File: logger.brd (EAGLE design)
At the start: 99 x 44.1 mm, 69 parts, among them IC1 LTC4412, J1 POWER_JACKPTH, Q1 FDN360P, Q2 FDN360P, Q3 2N7002PW, Q4 2N7002PW, U1 FT232RL

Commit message: Vcl attached to clock power and communication
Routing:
- net VDD: track 143.4 -> 128.8 mm, vias 3 -> 5
- net VCL: track 22.8 -> 29.2 mm
- net GND: vias 43 -> 48

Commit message: Vcl attached to clock power and communication
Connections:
- new net D4-SENSE_3V3_SWITCH: MCU.2, SENSE.3, TPS6122.6
- net D6-CLOCK_3V3_SWITCH: no longer MCU.2, SENSE.3, TPS6122.6
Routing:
- net D4-SENSE_3V3_SWITCH: track 0.00 -> 97.8 mm, vias 0 -> 6
- net D6-CLOCK_3V3_SWITCH: track 45.7 -> 43.3 mm, vias 4 -> 8
- net GND: vias 48 -> 50
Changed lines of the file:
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@@
 </signal>
 <signal name="D6-CLOCK_3V3_SWITCH">
-<contactref element="SENSE" pad="3"/>
-<contactref element="MCU" pad="2"/>
 <contactref element="CLOCK" pad="3"/>
 <contactref element="MCU" pad="10"/>
-<contactref element="TPS6122" pad="6"/>
-<wire x1="70.866" y1="15.8496" x2="71.4756" y2="15.8496" width="0.2032" layer="1"/>
-<wire x1="69.6468" y1="17.0688" x2="70.866" y2="15.8496" width="0.2032" layer="1"/>
-<wire x1="62.9412" y1="17.0688" x2="69.6468" y2="17.0688" width="0.2032" layer="1"/>
-<wire x1="60.5028" y1="17.0688" x2="62.9412" y2="17.0688" width="0.2032" layer="16"/>
-<wire x1="59.7408" y1="17.0688" x2="60.5028" y2="17.0688" width="0.2032" layer="1"/>
-<wire x1="57.3024" y1="14.6304" x2="59.7408" y2="17.0688" width="0.2032" layer="1"/>
-<wire x1="55.7784" y1="14.6304" x2="57.3024" y2="14.6304" width="0.2032" layer="1"/>
-<wire x1="55.3212" y1="14.1732" x2="55.7784" y2="14.6304" width="0.2032" layer="16"/>
-<wire x1="53.9369" y1="14.8082" x2="55.3212" y2="14.1732" width="0.2032" layer="16"/>
-<wire x1="53.9623" y1="14.8082" x2="53.9369" y2="14.8082" width="0.2032" layer="1"/>
-<wire x1="53.1876" y1="13.716" x2="53.9623" y2="14.8082" width="0.2032" layer="1"/>
-<wire x1="71.4756" y1="15.8496" x2="71.5516" y2="15.7663" width="0.2032" layer="1"/>
+<wire x1="54.2544" y1="14.7828" x2="53.1876" y2="13.716" width="0.2032" layer="1"/>
+<wire x1="55.626" y1="14.7828" x2="54.2544" y2="14.7828" width="0.2032" layer="16"/>
+<wire x1="55.7784" y1="14.6304" x2="55.626" y2="14.7828" width="0.2032" layer="16"/>
+<wire x1="57.3024" y1="14.6304" x2="55.7784" y2="14.6304" width="0.2032" layer="1"/>
+<wire x1="59.5884" y1="16.9164" x2="57.3024" y2="14.6304" width="0.2032" layer="1"/>
+<wire x1="60.5028" y1="16.9164" x2="59.5884" y2="16.9164" width="0.2032" layer="1"/>
+<wire x1="62.9412" y1="16.9164" x2="60.5028" y2="16.9164" width="0.2032" layer="16"/>
+<wire x1="62.9412" y1="19.9644" x2="62.9412" y2="16.9164" width="0.2032" layer="1"/>
+<wire x1="62.9412" y1="22.2504" x2="62.9412" y2="19.9644" width="0.2032" layer="16"/>
+<wire x1="61.2648" y1="23.9268" x2="62.9412" y2="22.2504" width="0.2032" layer="16"/>
+<wire x1="61.2648" y1="30.7848" x2="61.2648" y2="23.9268" width="0.2032" layer="16"/>
+<wire x1="60.5028" y1="31.5468" x2="61.2648" y2="30.7848" width="0.2032" layer="16"/>
+<wire x1="58.674" y1="31.5468" x2="60.5028" y2="31.5468" width="0.2032" layer="1"/>
+<wire x1="53.9496" y1="26.8224" x2="58.674" y2="31.5468" width="0.2032" layer="1"/>
+<wire x1="51.9684" y1="26.8224" x2="53.9496" y2="26.8224" width="0.2032" layer="1"/>
+<wire x1="51.3588" y1="26.2128" x2="51.9684" y2="26.8224" width="0.2032" layer="1"/>
+<wire x1="51.3588" y1="24.0792" x2="51.3588" y2="26.2128" width="0.2032" layer="16"/>
+<wire x1="50.4444" y1="23.1648" x2="51.3588" y2="24.0792" width="0.2032" layer="16"/>
+<wire x1="49.8348" y1="23.7744" x2="50.4444" y2="23.1648" width="0.2032" layer="1"/>
+<wire x1="49.8348" y1="24.384" x2="49.8348" y2="23.7744" width="0.2032" layer="1"/>
 <wire x1="53.1876" y1="13.716" x2="53.0525" y2="13.65" width="0.2032" layer="1"/>
-<wire x1="40.5384" y1="14.0462" x2="40.0812" y2="13.4112" width="0.2032" layer="1"/>
-<wire x1="43.8912" y1="16.764" x2="40.5384" y2="14.0462" width="0.2032" layer="1"/>
-<wire x1="44.5008" y1="16.764" x2="43.8912" y2="16.764" width="0.2032" layer="1"/>
-<wire x1="47.117" y1="18.7452" x2="46.482" y2="18.2245" width="0.2032" layer="1"/>
-<wire x1="46.482" y1="18.2245" x2="45.72" y2="17.145" width="0.2032" layer="1"/>
-<wire x1="45.72" y1="17.145" x2="44.5008" y2="16.764" width="0.2032" layer="1"/>
-<wire x1="50.9016" y1="18.7452" x2="49.8348" y2="18.7452" width="0.2032" layer="1"/>
-<wire x1="49.8348" y1="18.7452" x2="47.117" y2="18.7452" width="0.2032" layer="1"/>
-<wire x1="51.3588" y1="18.288" x2="50.9016" y2="18.7452" width="0.2032" layer="1"/>
-<wire x1="51.9684" y1="18.288" x2="51.3588" y2="18.288" width="0.2032" layer="1"/>
-<wire x1="40.0812" y1="13.4112" x2="40.035" y2="13.3325" width="0.2032" layer="1"/>
-<wire x1="51.9684" y1="18.288" x2="52.0827" y2="18.1676" width="0.2032" layer="1"/>
-<wire x1="49.8348" y1="18.7452" x2="49.8348" y2="24.384" width="0.2032" layer="1"/>
 <wire x1="49.8348" y1="24.384" x2="49.7901" y2="24.4602" width="0.2032" layer="1"/>
-<wire x1="53.9369" y1="14.7574" x2="53.9369" y2="14.8082" width="0.2032" layer="1"/>
-<wire x1="53.7972" y1="15.8496" x2="53.9369" y2="14.7574" width="0.2032" layer="1"/>
-<wire x1="53.7972" y1="17.0688" x2="53.7972" y2="15.8496" width="0.2032" layer="1"/>
-<wire x1="52.7304" y1="18.1356" x2="53.7972" y2="17.0688" width="0.2032" layer="1"/>
-<wire x1="52.1208" y1="18.1356" x2="52.7304" y2="18.1356" width="0.2032" layer="1"/>
-<wire x1="52.1208" y1="18.1356" x2="52.0827" y2="18.1676" width="0.2032" layer="1"/>
-<via x="62.9412" y="17.0688" extent="1-16" drill="0.3048"/>
-<via x="60.5028" y="17.0688" extent="1-16" drill="0.3048"/>
+<via x="54.2544" y="14.7828" extent="1-16" drill="0.3048"/>
 <via x="55.7784" y="14.6304" extent="1-16" drill="0.3048"/>
-<via x="53.9369" y="14.8082" extent="1-16" drill="0.3048"/>
+<via x="60.5028" y="16.9164" extent="1-16" drill="0.3048"/>
+<via x="62.9412" y="16.9164" extent="1-16" drill="0.3048"/>
+<via x="62.9412" y="19.9644" extent="1-16" drill="0.3048"/>
+<via x="60.5028" y="31.5468" extent="1-16" drill="0.3048"/>
+<via x="51.3588" y="26.2128" extent="1-16" drill="0.3048"/>
+<via x="50.4444" y="23.1648" extent="1-16" drill="0.3048"/>
 </signal>
 <signal name="LED+">
@@
 <via x="32.385" y="8.5725" extent="1-16" drill="0.3048" shape="octagon"/>
 <via x="80.3275" y="13.0175" extent="1-16" drill="0.3048" shape="octagon"/>
+<via x="37.1475" y="6.35" extent="1-16" drill="0.3048" shape="octagon"/>
+<via x="52.705" y="33.3375" extent="1-16" drill="0.3048" shape="octagon"/>
 </signal>
 <signal name="5V">
@@
 <via x="62.9412" y="13.1064" extent="1-16" drill="0.3048"/>
 </signal>
+<signal name="D4-SENSE_3V3_SWITCH">
+<contactref element="TPS6122" pad="6"/>
+<contactref element="MCU" pad="2"/>
+<contactref element="SENSE" pad="3"/>
+<wire x1="70.866" y1="15.8496" x2="71.4756" y2="15.8496" width="0.2032" layer="1"/>
+<wire x1="69.342" y1="17.3736" x2="70.866" y2="15.8496" width="0.2032" layer="1"/>
+<wire x1="69.342" y1="37.338" x2="69.342" y2="17.3736" width="0.2032" layer="16"/>
+<wire x1="63.0936" y1="43.5864" x2="69.342" y2="37.338" width="0.2032" layer="16"/>
+<wire x1="44.8056" y1="43.5864" x2="63.0936" y2="43.5864" width="0.2032" layer="16"/>
+<wire x1="41.7576" y1="40.5384" x2="44.8056" y2="43.5864" width="0.2032" layer="16"/>
+<wire x1="41.7576" y1="35.6616" x2="41.7576" y2="40.5384" width="0.2032" layer="16"/>
+<wire x1="41.6052" y1="35.5092" x2="41.7576" y2="35.6616" width="0.2032" layer="16"/>
+<wire x1="41.6052" y1="34.7472" x2="41.6052" y2="35.5092" width="0.2032" layer="1"/>
+<wire x1="44.8056" y1="31.5468" x2="41.6052" y2="34.7472" width="0.2032" layer="1"/>
+<wire x1="44.8056" y1="30.6324" x2="44.8056" y2="31.5468" width="0.2032" layer="16"/>
+<wire x1="43.8912" y1="29.718" x2="44.8056" y2="30.6324" width="0.2032" layer="16"/>
+<wire x1="44.196" y1="29.718" x2="43.8912" y2="29.718" width="0.2032" layer="1"/>
+<wire x1="44.3484" y1="29.5656" x2="44.196" y2="29.718" width="0.2032" layer="1"/>
+<wire x1="46.482" y1="29.5656" x2="44.3484" y2="29.5656" width="0.2032" layer="1"/>
+<wire x1="46.6344" y1="29.4132" x2="46.482" y2="29.5656" width="0.2032" layer="1"/>
+<wire x1="47.3964" y1="29.4132" x2="46.6344" y2="29.4132" width="0.2032" layer="16"/>
+<wire x1="50.4444" y1="26.3652" x2="47.3964" y2="29.4132" width="0.2032" layer="16"/>
+<wire x1="50.4444" y1="24.2316" x2="50.4444" y2="26.3652" width="0.2032" layer="16"/>
+<wire x1="49.6824" y1="23.4696" x2="50.4444" y2="24.2316" width="0.2032" layer="16"/>
+<wire x1="49.6824" y1="20.7264" x2="49.6824" y2="23.4696" width="0.2032" layer="16"/>
+<wire x1="49.6824" y1="19.9644" x2="49.6824" y2="20.7264" width="0.2032" layer="1"/>
+<wire x1="51.3588" y1="18.288" x2="50.9016" y2="18.7452" width="0.2032" layer="1"/>
+<wire x1="50.9016" y1="18.7452" x2="49.6824" y2="19.9644" width="0.2032" layer="1"/>
+<wire x1="51.9684" y1="18.288" x2="51.3588" y2="18.288" width="0.2032" layer="1"/>
+<wire x1="71.4756" y1="15.8496" x2="71.5516" y2="15.7663" width="0.2032" layer="1"/>
+<wire x1="51.9684" y1="18.288" x2="52.0827" y2="18.1676" width="0.2032" layer="1"/>
+<wire x1="42.3672" y1="15.6972" x2="40.0812" y2="13.4112" width="0.2032" layer="1"/>
+<wire x1="42.8244" y1="15.6972" x2="42.3672" y2="15.6972" width="0.2032" layer="1"/>
+<wire x1="43.8912" y1="16.764" x2="42.8244" y2="15.6972" width="0.2032" layer="1"/>
+<wire x1="44.5008" y1="16.764" x2="43.8912" y2="16.764" width="0.2032" layer="1"/>
+<wire x1="44.8056" y1="17.0688" x2="44.5008" y2="16.764" width="0.2032" layer="1"/>
+<wire x1="45.5676" y1="17.0688" x2="44.8056" y2="17.0688" width="0.2032" layer="1"/>
+<wire x1="47.244" y1="18.7452" x2="45.5676" y2="17.0688" width="0.2032" layer="1"/>
+<wire x1="50.9016" y1="18.7452" x2="47.244" y2="18.7452" width="0.2032" layer="1"/>
+<wire x1="40.0812" y1="13.4112" x2="40.035" y2="13.3325" width="0.2032" layer="1"/>
+<via x="69.342" y="17.3736" extent="1-16" drill="0.3048"/>
+<via x="41.6052" y="35.5092" extent="1-16" drill="0.3048"/>
+<via x="44.8056" y="31.5468" extent="1-16" drill="0.3048"/>
+<via x="43.8912" y="29.718" extent="1-16" drill="0.3048"/>
+<via x="46.6344" y="29.4132" extent="1-16" drill="0.3048"/>
+<via x="49.6824" y="20.7264" extent="1-16" drill="0.3048"/>
+</signal>
 </signals>

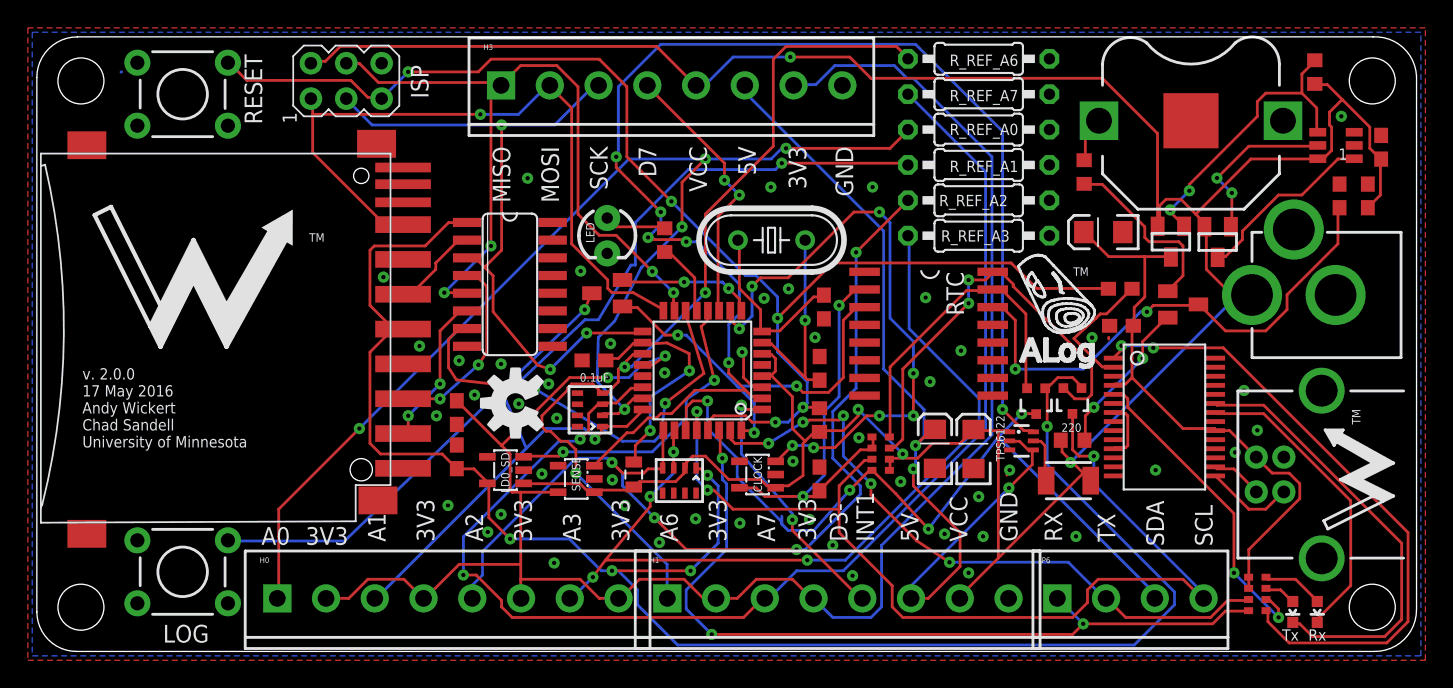
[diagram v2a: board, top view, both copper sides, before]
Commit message: Straighten traces
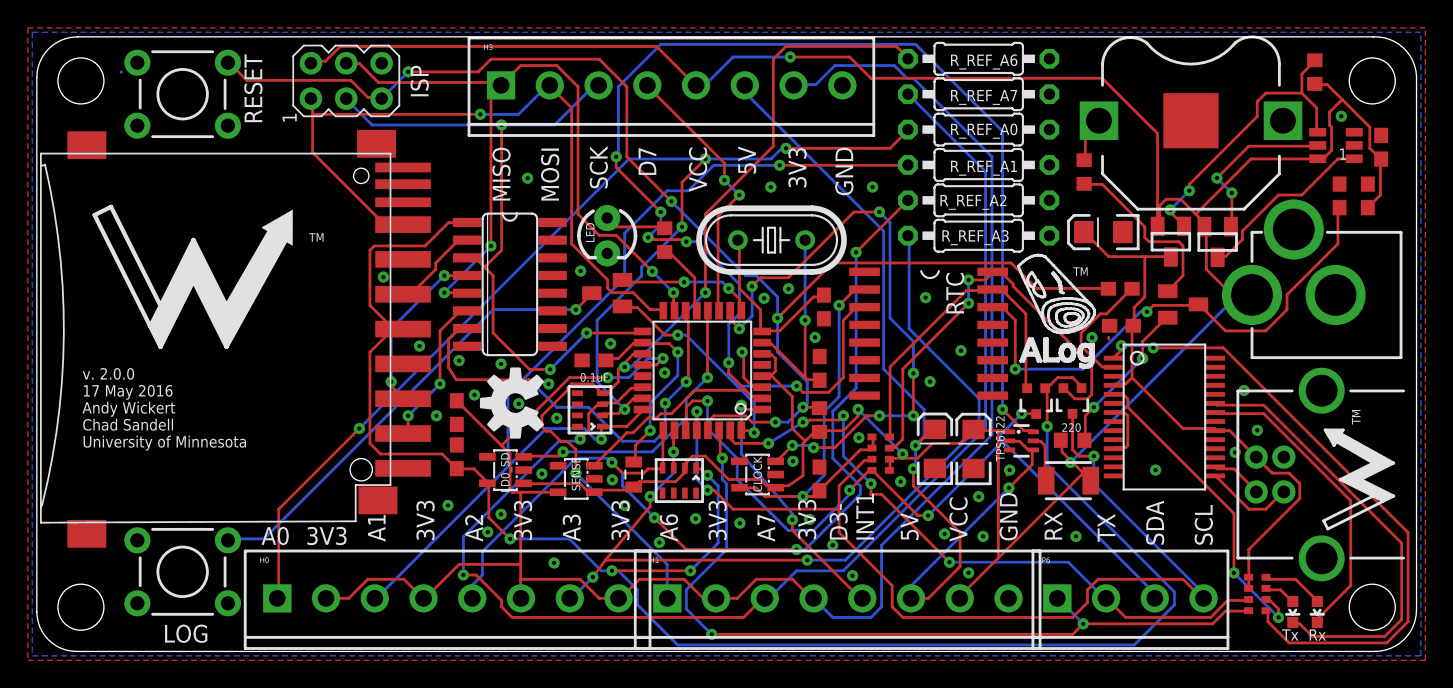
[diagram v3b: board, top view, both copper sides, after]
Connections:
- net D4-SENSE_3V3_SWITCH renamed D4-SENSE_LDO_SWITCH
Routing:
- net SDA: track 57.3 -> 55.8 mm
- net SD_DI: track 13.9 -> 12.4 mm
- net AVCC: track 16.5 -> 15.2 mm
- net CLK: track 49.5 -> 50.3 mm
- net A1: track 68.1 -> 68.6 mm
- net CS-SD: track 31.2 -> 31.6 mm, vias 2 -> 3

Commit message: Charge pump
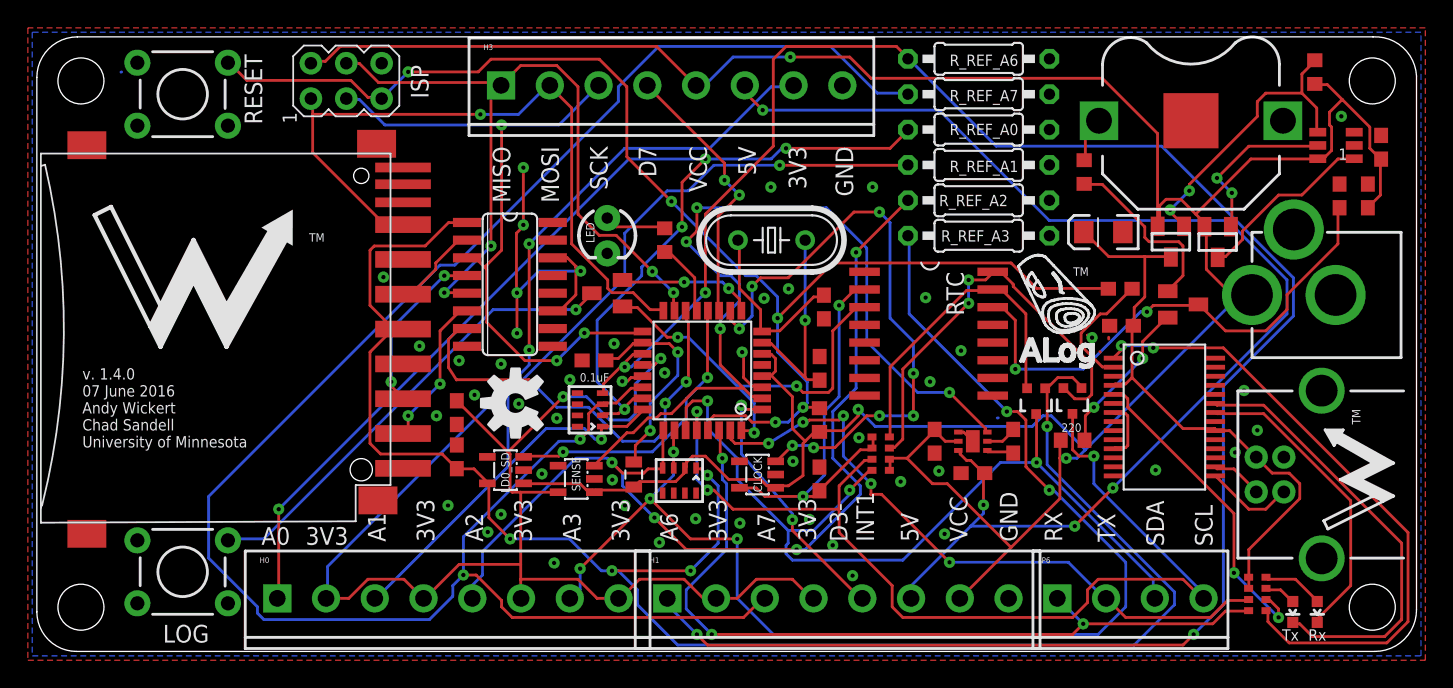
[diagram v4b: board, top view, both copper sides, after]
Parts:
- removed C1, C2: 10uF, SparkFun-Passives:EIA3216
- removed L1: 4.7uH, SteveMarple:1210
- removed TPS6122: TPS6122TPS6122, csandell:SC70-6L
- added C_BOOST_1: 4.7uF, resistor:C0603
- added C_BOOST_2, C_BOOST_3: 2.2uF, resistor:C0603
- added U2: TPS60150, ti_by_element14:SON65P200X200X80-7N
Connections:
- removed net N$12: L1.1, TPS6122.5
- new net N$14: C_BOOST_2.2, U2.4
- new net N$15: C_BOOST_2.1, U2.5
- net 5V: now also C_BOOST_3.2, U2.3; no longer C2.A, TPS6122.2, TPS6122.4
- net D4-SENSE_LDO_SWITCH: now also U2.6; no longer TPS6122.6
- net GND: now also C_BOOST_1.1, C_BOOST_3.1, U2.1, U2.7; no longer C1.C, C2.C, TPS6122.3
- net VCC: now also C_BOOST_1.2, U2.2; no longer C1.A, L1.2, TPS6122.1
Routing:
- net A6: track 65.0 -> 144.4 mm, vias 3 -> 4
- net A7: track 91.7 -> 136.7 mm
- net D4-SENSE_LDO_SWITCH: track 97.8 -> 62.8 mm, vias 6 -> 4
- net A3: track 62.8 -> 91.7 mm, vias 4 -> 6
- net GND: track 9.22 -> 36.2 mm, vias 50 -> 49
- net 5V: track 64.2 -> 90.3 mm, vias 3 -> 4
- net VCC: track 212.5 -> 220.8 mm, vias 4 -> 3
- net SDA: track 55.8 -> 62.8 mm, vias 4 -> 3
- net N$12: track 3.53 -> 0.00 mm
- net N$15: track 0.00 -> 2.26 mm
- net N$14: track 0.00 -> 2.02 mm
- net +3V3: track 133.9 -> 132.3 mm, vias 2 -> 4
- net CLK: track 50.3 -> 49.6 mm
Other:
- board text added: "v. 1.4.0 07 June 2016 Andy Wickert Chad Sandell University of Minnesota"
- board text removed: "v. 2.0.0 17 May 2016 Andy Wickert Chad Sandell University of Minnesota"
